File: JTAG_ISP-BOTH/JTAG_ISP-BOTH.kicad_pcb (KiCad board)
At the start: 2 copper layers, 48.7 x 46.1 mm, 20 parts, among them J1 Conn_01x08, J1 Conn_02x03_Odd_Even, J2 Conn_01x08, J3 Conn_01x08

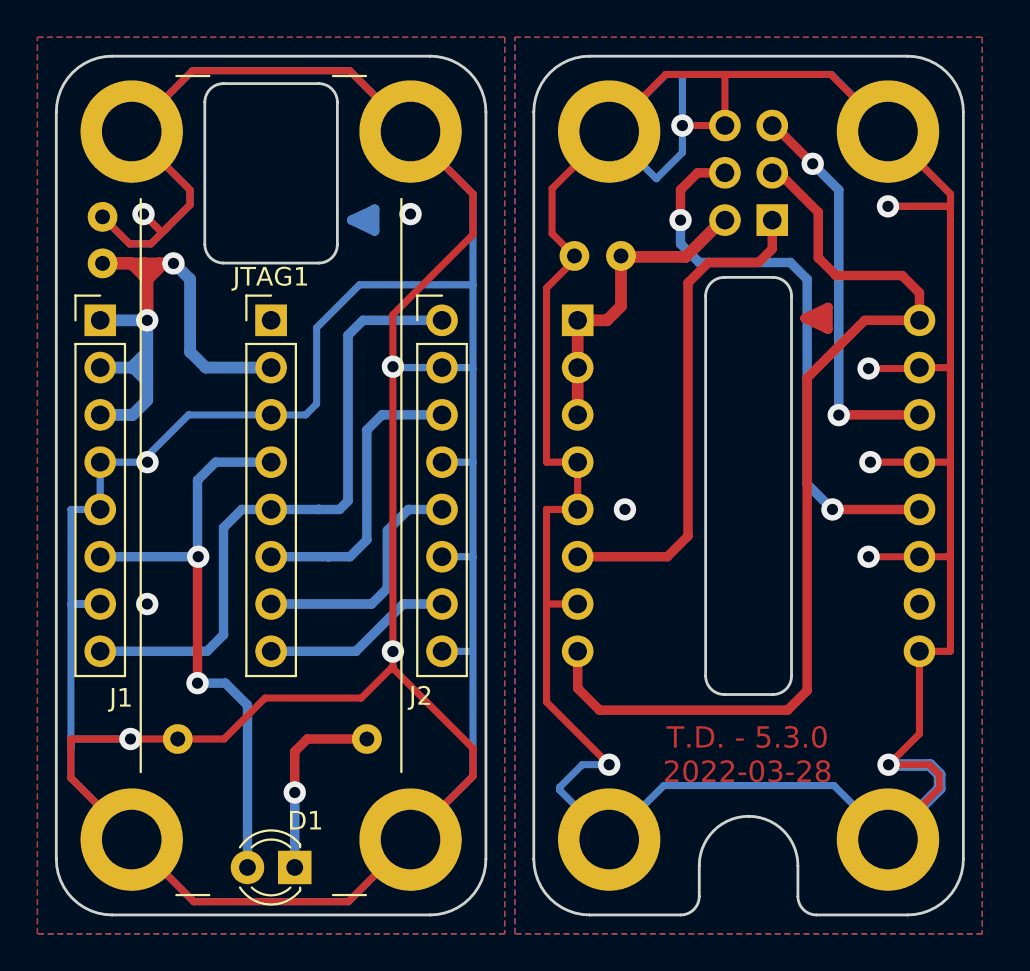
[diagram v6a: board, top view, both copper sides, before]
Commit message: # [PCB] + Création d'une archive PROD_LPKF.zip qui contient les fichiers envoyés pour fabrication. * Mise à jour des fichiers gerbers du projet BOTH. * Mise à jour de la cartouche pour le projet BOTH.     * Date actuelle;
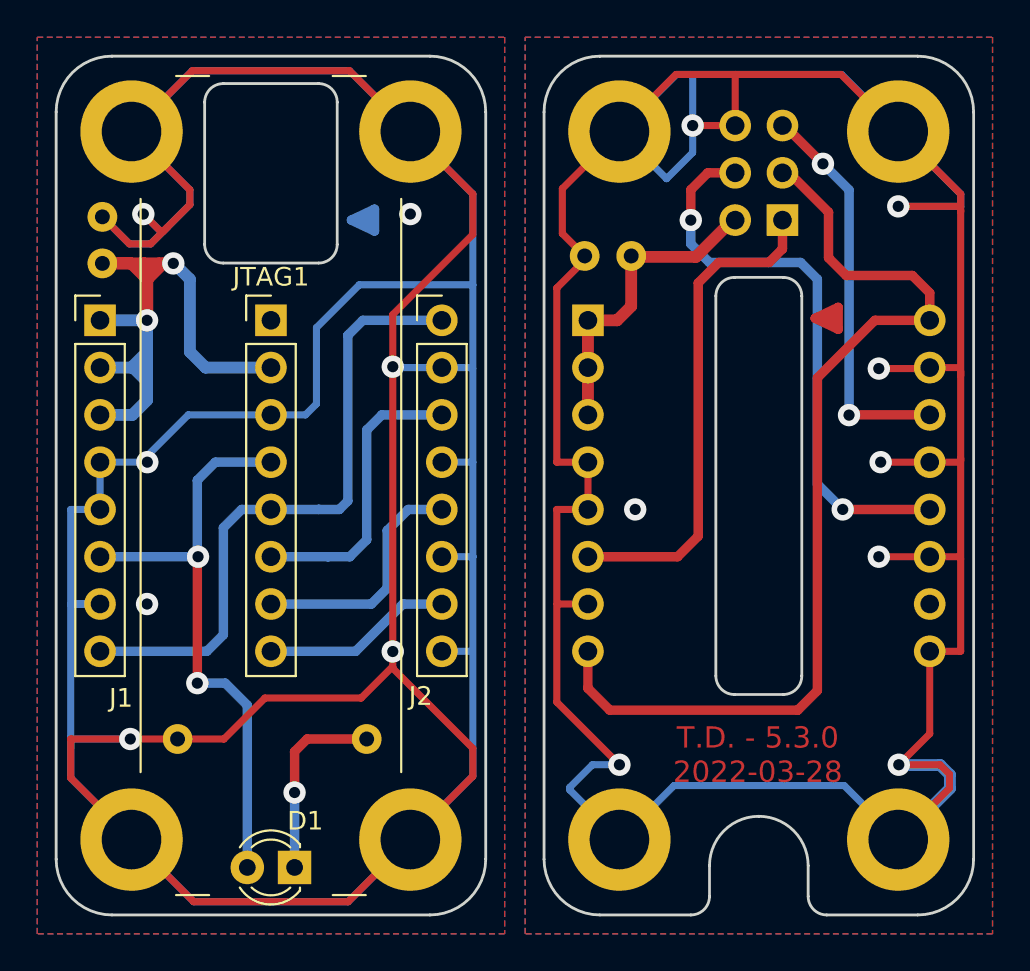
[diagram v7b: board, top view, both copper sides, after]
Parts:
- removed the C1 at (91.3, 56.3)
- removed the C1 at (119.2, 55.9)
- removed the J1 at (91.2, 59.3)
- removed the J1 at (127.3, 53.9)
- removed the J2 at (109.5, 59.3)
- removed the J2 at (116.8, 59.3)
- removed the REF** at (107.8, 49.2)
- removed the REF** at (105.9, 54.3)
- removed the REF** at (118.5, 87.2)
- removed the REF** at (92.9, 49.2)
- removed the REF** at (92.9, 87.2)
- removed the REF** at (130.3, 58.9)
- removed the REF** at (118.5, 49.2)
- removed the REF** at (107.8, 87.2)
- removed the REF** at (133.5, 87.2)
- removed the REF** at (133.5, 49.2)
- added C1: 100nF, Capacitor_THT:C_Disc_D3.0mm_W2.0mm_P2.50mm, B.Cu at (91.3, 56.3)
- added C1: 100nF, Capacitor_THT:C_Disc_D3.0mm_W2.0mm_P2.50mm, B.Cu at (119.7, 55.9)
- added J1: Conn_01x08, Connector_PinHeader_2.54mm:PinHeader_1x08_P2.54mm_Vertical, F.Cu at (91.2, 59.3)
- added J1: Conn_02x03_Odd_Even, Connector_PinSocket_2.54mm:PinSocket_2x03_P2.54mm_Vertical, B.Cu at (127.8, 53.9)
- added J2: Conn_01x08, Connector_PinHeader_2.54mm:PinHeader_1x08_P2.54mm_Vertical, F.Cu at (109.5, 59.3)
- added J2: Conn_01x08, Connector_PinHeader_2.54mm:PinHeader_1x08_P2.54mm_Vertical, B.Cu at (117.4, 59.3)
- added REF**: MountingHole_3.2mm_M3_ISO14580_Pad, MountingHole:MountingHole_3.2mm_M3_ISO14580_Pad, F.Cu at (107.8, 49.2)
- added REF**: Fleche_small, THOMAS_library:Fleche_small, B.Cu at (105.9, 54.3)
- added REF**: MountingHole_3.2mm_M3_ISO14580_Pad, MountingHole:MountingHole_3.2mm_M3_ISO14580_Pad, F.Cu at (134.0, 87.2)
- added REF**: MountingHole_3.2mm_M3_ISO14580_Pad, MountingHole:MountingHole_3.2mm_M3_ISO14580_Pad, F.Cu at (92.9, 49.2)
- added REF**: MountingHole_3.2mm_M3_ISO14580_Pad, MountingHole:MountingHole_3.2mm_M3_ISO14580_Pad, F.Cu at (134.0, 49.2)
- added REF**: MountingHole_3.2mm_M3_ISO14580_Pad, MountingHole:MountingHole_3.2mm_M3_ISO14580_Pad, F.Cu at (119.1, 49.2)
- added REF**: MountingHole_3.2mm_M3_ISO14580_Pad, MountingHole:MountingHole_3.2mm_M3_ISO14580_Pad, F.Cu at (119.1, 87.2)
- added REF**: MountingHole_3.2mm_M3_ISO14580_Pad, MountingHole:MountingHole_3.2mm_M3_ISO14580_Pad, F.Cu at (107.8, 87.2)
- added REF**: MountingHole_3.2mm_M3_ISO14580_Pad, MountingHole:MountingHole_3.2mm_M3_ISO14580_Pad, F.Cu at (92.9, 87.2)
- added REF**: Fleche_small, THOMAS_library:Fleche_small, F.Cu at (130.8, 58.9)
- moved J3 0.55 mm to (135.7, 59.3)
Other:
- board size 48.7 x 46.1 mm -> 49.3 x 46.1 mm
